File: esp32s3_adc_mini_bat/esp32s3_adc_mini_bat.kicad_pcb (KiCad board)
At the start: 2 copper layers, 42 x 52 mm, 39 parts, among them CN1 PJ-320D, J1 USB_C_Receptacle_USB2.0_16P, J4 Conn_01x22_Socket, J5 Conn_01x22_Socket, SW1 TS-1088-AR02016, SW2 TS-1088-AR02016, U1 USBLC6-2SC6, U2 ESP32-S3-WROOM-1, U3 AP2112K-3.3, U4 PCM1808PWR

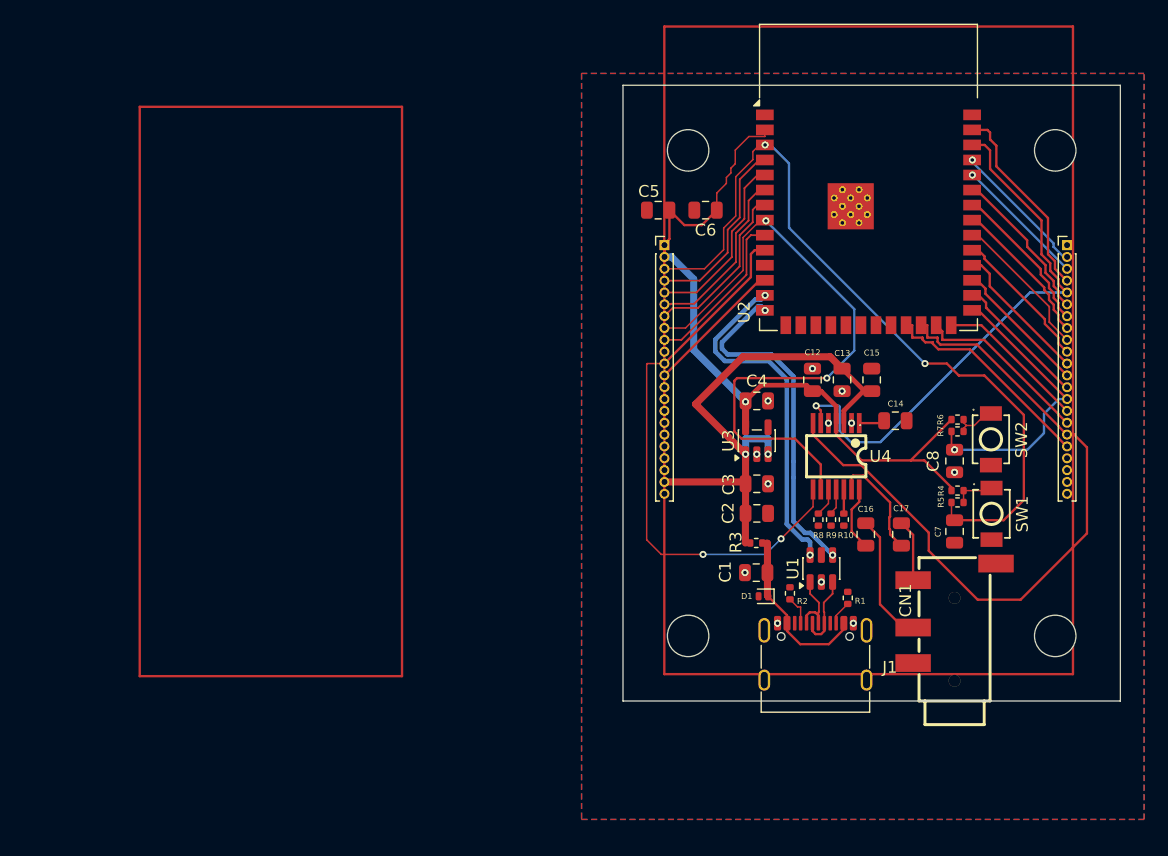
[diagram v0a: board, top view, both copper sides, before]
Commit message: feat: schematic done and pcb grouping
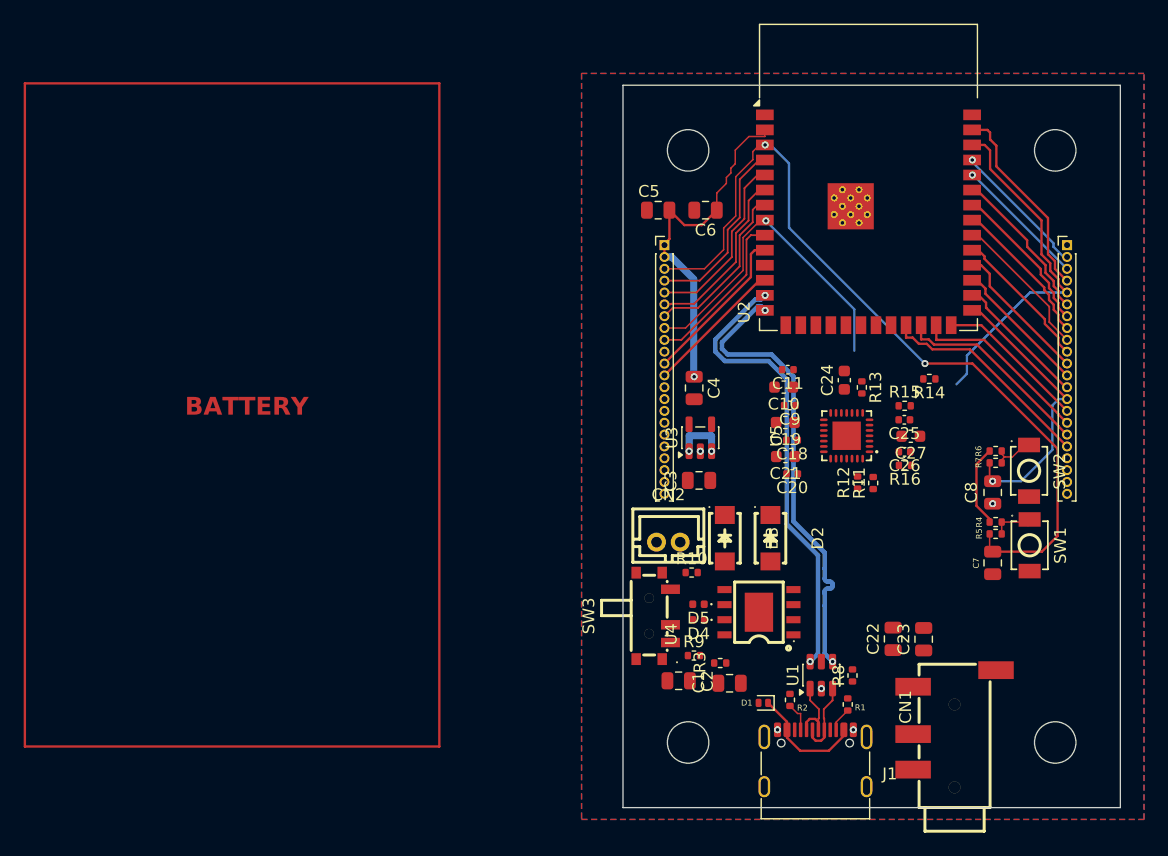
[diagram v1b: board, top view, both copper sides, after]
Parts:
- removed C12, C13, C14, C16, C17: 1u, Capacitor_SMD:C_0805_2012Metric
- removed C15: 10u, Capacitor_SMD:C_0805_2012Metric
- added C10: 10u, Capacitor_SMD:C_0603_1608Metric, F.Cu at (145.6, 82.5)
- added C11: 100n, Capacitor_SMD:C_0402_1005Metric, F.Cu at (145.9, 81.0)
- added C18: 100n, Capacitor_SMD:C_0402_1005Metric, F.Cu at (146.3, 87.0)
- added C19: 10u, Capacitor_SMD:C_0603_1608Metric, F.Cu at (145.7, 85.5)
- added C20: 100n, Capacitor_SMD:C_0402_1005Metric, F.Cu at (146.3, 89.8)
- added C21: 10u, Capacitor_SMD:C_0603_1608Metric, F.Cu at (145.7, 88.4)
- added C22: 1u, Capacitor_SMD:C_0805_2012Metric, F.Cu at (154.8, 103.8)
- added C23: 1u, Capacitor_SMD:C_0805_2012Metric, F.Cu at (157.4, 103.8)
- added C24: 10u, Capacitor_SMD:C_0603_1608Metric, F.Cu at (150.7, 81.9)
- added C25: 100n, Capacitor_SMD:C_0402_1005Metric, F.Cu at (155.8, 85.2)
- added C26: 100n, Capacitor_SMD:C_0402_1005Metric, F.Cu at (155.8, 88.0)
- added C27: 10u, Capacitor_SMD:C_0603_1608Metric, F.Cu at (156.3, 86.6)
- added C9: 100n, Capacitor_SMD:C_0402_1005Metric, F.Cu at (146.1, 84.0)
- added CN2: B2B-PH-K-S, easyeda2kicad:CONN-TH_B2B-PH-K-S, F.Cu at (135.8, 95.6)
- added D2: SS14, easyeda2kicad:SMA_L4.2-W2.6-LS5.0-RD_1, F.Cu at (144.4, 95.2)
- added D3: SS14, easyeda2kicad:SMA_L4.2-W2.6-LS5.0-RD_1, F.Cu at (140.6, 95.2)
- added D4: LED, LED_SMD:LED_0402_1005Metric, F.Cu at (138.4, 102.1)
- added D5: LED, LED_SMD:LED_0402_1005Metric, F.Cu at (138.4, 100.8)
- added R11: 10k, Resistor_SMD:R_0402_1005Metric, F.Cu at (153.1, 90.6)
- added R12: 10k, Resistor_SMD:R_0402_1005Metric, F.Cu at (151.8, 90.5)
- added R13: 33, Resistor_SMD:R_0402_1005Metric, F.Cu at (152.2, 82.5)
- added R14: 33, Resistor_SMD:R_0402_1005Metric, F.Cu at (157.9, 81.8)
- added R15: 33, Resistor_SMD:R_0402_1005Metric, F.Cu at (155.8, 84.1)
- added R16: 33, Resistor_SMD:R_0402_1005Metric, F.Cu at (155.8, 89.1)
- added SW3: XDMK-12C01-25, easyeda2kicad:SW-SMD_XDMK-12C01-25, F.Cu at (134.6, 101.8)
- added U5: ES8388, easyeda2kicad:QFN-28_L4.0-W4.0-P0.45-BL-EP, F.Cu at (150.9, 86.6)
- R10, R9: value 10k -> 560
- R8: value 10k -> 3.6k
- U4: value PCM1808PWR -> TP4056_C382139; footprint easyeda2kicad:TSSOP-14_L5.0-W4.4-P0.65-LS6.4-BL -> easyeda2kicad:ESOP-8_L4.9-W3.9-P1.27-LS6.0-BL-EP
- moved R9 16.3 mm to (138.0, 105.2), turned to 0 degrees
- moved C2 15.6 mm to (136.7, 107.3), turned to 180 degrees
- moved U4 14.7 mm to (143.5, 101.5), turned to 90 degrees
- moved R10 13.6 mm to (137.8, 98.2), turned to 0 degrees
- moved R8 13.5 mm to (151.4, 106.8), turned to 90 degrees
- moved R3 10.6 mm to (140.2, 105.8)
- moved C1 9.61 mm to (141.0, 107.5)
- moved CN1 9.00 mm to (160.0, 110.6)
- moved D1 9.00 mm to (143.8, 109.2)
- moved H3 9.00 mm to (168.5, 112.5)
- moved H4 9.00 mm to (137.5, 112.5)
- moved J1 9.00 mm to (148.2, 115.2)
- moved R1 9.00 mm to (151.0, 109.3)
- moved R2 9.00 mm to (146.1, 108.9)
- moved U1 9.00 mm to (148.8, 106.8)
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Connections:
- net IO8 renamed I2C_DAT
- C1 pad 1: VBUS -> Net-(D1-K)
- C2 pad 1: +5V -> VBUS
- C3 pad 1: +5V -> LDO_IN
- D1 pad 1: VBUS -> Net-(D1-K)
- J1 pad A4: VBUS -> Net-(D1-K)
- J1 pad A9: VBUS -> Net-(D1-K)
- J1 pad B4: VBUS -> Net-(D1-K)
- J1 pad B9: VBUS -> Net-(D1-K)
- J4 pad 21: +5V -> VBUS
- R10 pad 1: Net-(U4-FMT) -> Net-(D5-A)
- R10 pad 2: GND -> VBUS
- R3 pad 1: VBUS -> Net-(D1-K)
- R3 pad 2: +5V -> VBUS
- R8 pad 1: Net-(U4-MD0) -> GND
- R8 pad 2: GND -> Net-(U4-PROG)
- R9 pad 1: Net-(U4-MD1) -> Net-(D4-A)
- R9 pad 2: GND -> VBUS
- U2 pad 11: IO18 -> I2C_CLK
- U3 pad 1: +5V -> LDO_IN
- U3 pad 3: +5V -> LDO_IN
- U4 pad 1: Net-(U4-VREF) -> GND
- U4 pad 2: GND -> Net-(U4-PROG)
- U4 pad 3: +5V -> GND
- U4 pad 4: +3V3 -> VBUS
- U4 pad 5: GND -> Net-(D3-A)
- U4 pad 6: SCKI -> Net-(D5-K)
- U4 pad 7: LRCK -> Net-(D4-K)
- U4 pad 8: BCK -> VBUS
- U4 pad 9: DOUT -> GND
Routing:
- net +5V: track 46.7 -> 0.00 mm, vias 2 -> 0
- net LRCK: track 59.5 -> 16.9 mm
- net BCK: track 47.7 -> 13.6 mm, vias 2 -> 0
- net +3V3: track 64.2 -> 36.9 mm
- net DOUT: track 54.5 -> 28.5 mm, vias 2 -> 1
- net SCKI: track 47.1 -> 30.0 mm, vias 1 -> 0
- net VBUS: track 14.5 -> 0.00 mm
- net LINE-IN-R: track 11.0 -> 0.00 mm
- net Net-(D1-K): track 0.00 -> 9.88 mm
- net USB_D+: track 29.3 -> 39.0 mm
- net Net-(U4-VINL): track 9.40 -> 0.00 mm
- net USB_D-: track 29.7 -> 39.0 mm
- net Net-(U4-VINR): track 5.51 -> 0.00 mm
- net LINE-IN-L: track 5.22 -> 0.00 mm
- net LDO_IN: track 0.00 -> 4.49 mm, vias 0 -> 2
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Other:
- board size 42 x 52 mm -> 42 x 61 mm
- board text added: "BATTERY"
